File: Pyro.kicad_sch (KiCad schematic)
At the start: 31 parts, among them J12 Conn_01x02_Male, Q1 SSM3K15AMFV,L3F, Q2 BUK9M11-40EX, U6 SiC437BED-T1-GE3, U8 TPS259621DDAT, U9 LTV-247

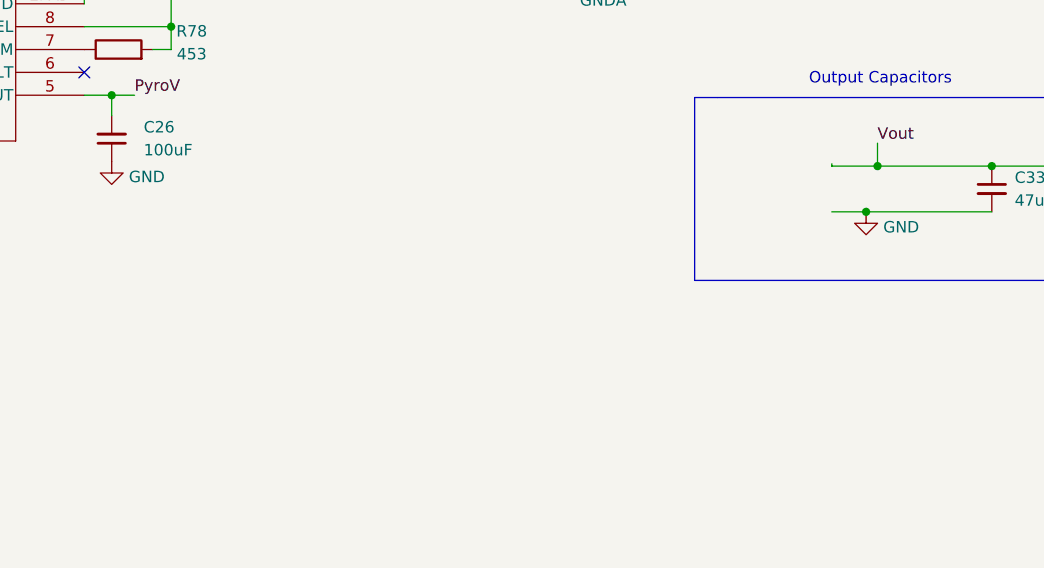
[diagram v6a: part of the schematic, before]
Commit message: added pyro buck caps
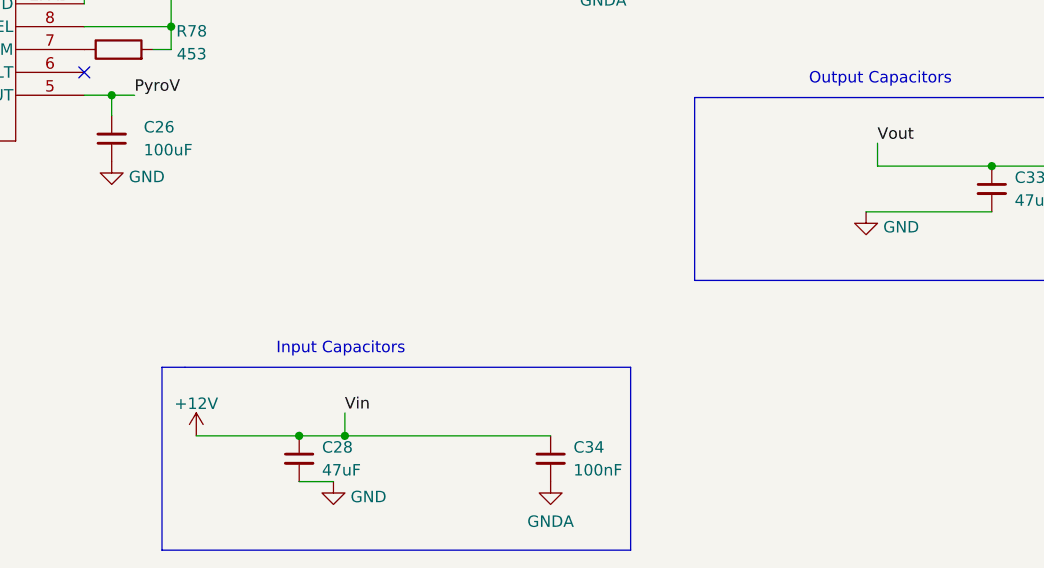
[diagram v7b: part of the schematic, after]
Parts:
- added C28: 47uF, Capacitor_SMD:C_1206_3216Metric, symbol Device:C_Small
- added C34: 100nF, Capacitor_SMD:C_0402_1005Metric, symbol Device:C_Small
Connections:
- net +12V: now also C28.1, C34.1
- net GND: now also C28.2, C34.2
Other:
- note added: "Input Capacitors"
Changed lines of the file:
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@@
   (junction (at 103.378 55.626) (diameter 0) (color 0 0 0 0)
   )
-  (junction (at 186.944 130.302) (diameter 0) (color 0 0 0 0)
-  )
   (junction (at 101.854 122.428) (diameter 0) (color 0 0 0 0)
   )
@@
   (junction (at 157.734 101.092) (diameter 0) (color 0 0 0 0)
   )
+  (junction (at 127.762 160.274) (diameter 0) (color 0 0 0 0)
+  )
   (junction (at 174.244 83.312) (diameter 0) (color 0 0 0 0)
   )
@@
   (junction (at 80.518 32.766) (diameter 0) (color 0 0 0 0)
   )
-  (junction (at 185.674 135.382) (diameter 0) (color 0 0 0 0)
-  )
   (junction (at 28.702 93.218) (diameter 0) (color 0 0 0 0)
   )
@@
   )
   (junction (at 32.004 126.492) (diameter 0) (color 0 0 0 0)
+  )
+  (junction (at 122.682 160.274) (diameter 0) (color 0 0 0 0)
   )
   (junction (at 110.998 73.406) (diameter 0) (color 0 0 0 0)
@@
     (stroke (width 0) (type default))
   )
+  (polyline (pts (xy 159.512 152.654) (xy 159.512 172.974))
+    (stroke (width 0) (type default))
+  )
   (wire (pts (xy 174.244 83.312) (xy 174.244 85.852))
     (stroke (width 0) (type default))
@@
     (stroke (width 0) (type default))
   )
-  (wire (pts (xy 181.864 135.382) (xy 185.674 135.382))
-    (stroke (width 0) (type default))
-  )
   (wire (pts (xy 118.618 72.136) (xy 118.618 73.406))
     (stroke (width 0) (type default))
@@
     (stroke (width 0) (type default))
   )
+  (wire (pts (xy 111.252 160.274) (xy 122.682 160.274))
+    (stroke (width 0) (type default))
+  )
   (wire (pts (xy 245.364 129.032) (xy 245.364 126.492))
     (stroke (width 0) (type default))
@@
     (stroke (width 0) (type default))
   )
-  (wire (pts (xy 181.864 130.048) (xy 181.864 130.302))
-    (stroke (width 0) (type default))
-  )
   (wire (pts (xy 161.544 70.612) (xy 174.244 70.612))
     (stroke (width 0) (type default))
@@
     (stroke (width 0) (type default))
   )
+  (polyline (pts (xy 109.982 152.654) (xy 159.512 152.654))
+    (stroke (width 0) (type default))
+  )
+  (polyline (pts (xy 159.512 172.974) (xy 107.442 172.974))
+    (stroke (width 0) (type default))
+  )
   (wire (pts (xy 231.394 83.312) (xy 230.124 83.312))
     (stroke (width 0) (type default))
   )
+  (wire (pts (xy 127.762 157.734) (xy 127.762 160.274))
+    (stroke (width 0) (type default))
+  )
   (wire (pts (xy 98.806 112.268) (xy 98.806 103.886))
     (stroke (width 0) (type default))
@@
     (stroke (width 0) (type default))
   )
+  (wire (pts (xy 122.682 160.274) (xy 127.762 160.274))
+    (stroke (width 0) (type default))
+  )
   (wire (pts (xy 47.498 63.246) (xy 47.498 64.516))
     (stroke (width 0) (type default))
@@
     (stroke (width 0) (type default))
   )
+  (polyline (pts (xy 107.442 152.654) (xy 109.982 152.654))
+    (stroke (width 0) (type default))
+  )
   (wire (pts (xy 240.284 126.492) (xy 245.364 126.492))
     (stroke (width 0) (type default))
@@
     (stroke (width 0) (type default))
   )
+  (polyline (pts (xy 107.442 172.974) (xy 107.442 152.654))
+    (stroke (width 0) (type default))
+  )
+  (wire (pts (xy 127.762 160.274) (xy 150.622 160.274))
+    (stroke (width 0) (type default))
+  )
   (wire (pts (xy 18.542 93.218) (xy 28.702 93.218))
     (stroke (width 0) (type default))
@@
     (stroke (width 0) (type default))
   )
-  (wire (pts (xy 181.864 130.302) (xy 186.944 130.302))
-    (stroke (width 0) (type default))
-  )
   (wire (pts (xy 23.876 103.886) (xy 23.876 105.41))
     (stroke (width 0) (type default))
@@
   )
   (wire (pts (xy 95.758 55.626) (xy 103.378 55.626))
+    (stroke (width 0) (type default))
+  )
+  (wire (pts (xy 122.682 165.354) (xy 126.492 165.354))
     (stroke (width 0) (type default))
   )
@@
     (effects (font (size 1.27 1.27)) (justify left bottom))
   )
+  (text "Input Capacitors\n" (at 120.142 151.384 0)
+    (effects (font (size 1.27 1.27)) (justify left bottom))
+  )
   (text "Output Capacitors\n" (at 179.324 121.412 0)
     (effects (font (size 1.27 1.27)) (justify left bottom))
@@
   )
   (label "VDD" (at 241.554 75.692 0) (fields_autoplaced)
+    (effects (font (size 1.27 1.27)) (justify left bottom))
+  )
+  (label "Vin" (at 127.762 157.734 0) (fields_autoplaced)
     (effects (font (size 1.27 1.27)) (justify left bottom))
   )
@@
         (path "/7db990e4-92e1-4f99-b4d2-435bbec1ba83/3c6662b6-8783-49dc-b944-3dc2b3e30a07"
           (reference "#PWR0157") (unit 1)
+        )
+      )
+    )
+  )
+  (symbol (lib_id "power:GND") (at 126.492 165.354 0) (unit 1)
+    (in_bom yes) (on_board yes) (dnp no) (fields_autoplaced)
+    (property "Reference" "#PWR064" (at 126.492 171.704 0)
+      (effects (font (size 1.27 1.27)) hide)
+    )
+    (property "Value" "GND" (at 128.397 167.0578 0)
+      (effects (font (size 1.27 1.27)) (justify left))
+    )
+    (property "Footprint" "" (at 126.492 165.354 0)
+      (effects (font (size 1.27 1.27)) hide)
+    )
+    (property "Datasheet" "" (at 126.492 165.354 0)
+      (effects (font (size 1.27 1.27)) hide)
+    )
+    (pin "1")
+    (instances
+      (project "Ricardo-Stark"
+        (path "/7db990e4-92e1-4f99-b4d2-435bbec1ba83/6c17bf58-bab3-4fa6-ad33-cca9e388d73c"
+          (reference "#PWR064") (unit 1)
+        )
+        (path "/7db990e4-92e1-4f99-b4d2-435bbec1ba83/3c6662b6-8783-49dc-b944-3dc2b3e30a07"
+          (reference "#PWR0176") (unit 1)
         )
       )
@@
     )
   )
+  (symbol (lib_id "power:GNDA") (at 150.622 165.354 0) (unit 1)
+    (in_bom yes) (on_board yes) (dnp no) (fields_autoplaced)
+    (property "Reference" "#PWR066" (at 150.622 171.704 0)
+      (effects (font (size 1.27 1.27)) hide)
+    )
+    (property "Value" "GNDA" (at 150.622 169.7974 0)
+      (effects (font (size 1.27 1.27)))
+    )
+    (property "Footprint" "" (at 150.622 165.354 0)
+      (effects (font (size 1.27 1.27)) hide)
+    )
+    (property "Datasheet" "" (at 150.622 165.354 0)
+      (effects (font (size 1.27 1.27)) hide)
+    )
+    (pin "1")
+    (instances
+      (project "Ricardo-Stark"
+        (path "/7db990e4-92e1-4f99-b4d2-435bbec1ba83/6c17bf58-bab3-4fa6-ad33-cca9e388d73c"
+          (reference "#PWR066") (unit 1)
+        )
+        (path "/7db990e4-92e1-4f99-b4d2-435bbec1ba83/3c6662b6-8783-49dc-b944-3dc2b3e30a07"
+          (reference "#PWR0177") (unit 1)
+        )
+      )
+    )
+  )
   (symbol (lib_id "power:GND") (at 221.234 93.472 0) (unit 1)
     (in_bom yes) (on_board yes) (dnp no) (fields_autoplaced)
@@
     )
   )
+  (symbol (lib_id "Device:C_Small") (at 150.622 162.814 0) (unit 1)
+    (in_bom yes) (on_board yes) (dnp no) (fields_autoplaced)
+    (property "Reference" "C34" (at 153.162 161.5503 0)
+      (effects (font (size 1.27 1.27)) (justify left))
+    )
+    (property "Value" "100nF" (at 153.162 164.0903 0)
+      (effects (font (size 1.27 1.27)) (justify left))
+    )
+    (property "Footprint" "Capacitor_SMD:C_0402_1005Metric" (at 150.622 162.814 0)
+      (effects (font (size 1.27 1.27)) hide)
+    )
+    (property "Datasheet" "~" (at 150.622 162.814 0)
+      (effects (font (size 1.27 1.27)) hide)
+    )
+    (pin "1")
+    (pin "2")
+    (instances
+      (project "Ricardo-Stark"
+        (path "/7db990e4-92e1-4f99-b4d2-435bbec1ba83/6c17bf58-bab3-4fa6-ad33-cca9e388d73c"
+          (reference "C34") (unit 1)
+        )
+        (path "/7db990e4-92e1-4f99-b4d2-435bbec1ba83/3c6662b6-8783-49dc-b944-3dc2b3e30a07"
+          (reference "C83") (unit 1)
+        )
+      )
+    )
+  )
   (symbol (lib_id "power:+3V3") (at 98.298 50.546 0) (unit 1)
     (in_bom yes) (on_board yes) (dnp no) (fields_autoplaced)
@@
         )
       )
+    )
+  )
+  (symbol (lib_id "Device:C_Small") (at 122.682 162.814 0) (unit 1)
+    (in_bom yes) (on_board yes) (dnp no) (fields_autoplaced)
+    (property "Reference" "C28" (at 125.222 161.5503 0)
+      (effects (font (size 1.27 1.27)) (justify left))
+    )
+    (property "Value" "47uF" (at 125.222 164.0903 0)
+      (effects (font (size 1.27 1.27)) (justify left))
+    )
+    (property "Footprint" "Capacitor_SMD:C_1206_3216Metric" (at 122.682 162.814 0)
+      (effects (font (size 1.27 1.27)) hide)
+    )
+    (property "Datasheet" "~" (at 122.682 162.814 0)
+      (effects (font (size 1.27 1.27)) hide)
+    )
+    (pin "1")
+    (pin "2")
+    (instances
+      (project "Ricardo-Stark"
+        (path "/7db990e4-92e1-4f99-b4d2-435bbec1ba83/6c17bf58-bab3-4fa6-ad33-cca9e388d73c"
+          (reference "C28") (unit 1)
+        )
+        (path "/7db990e4-92e1-4f99-b4d2-435bbec1ba83/3c6662b6-8783-49dc-b944-3dc2b3e30a07"
+          (reference "C80") (unit 1)
+        )
+      )
+    )
+  )
+  (symbol (lib_id "power:+12V") (at 111.252 160.274 0) (unit 1)
+    (in_bom yes) (on_board yes) (dnp no) (fields_autoplaced)
+    (property "Reference" "#PWR063" (at 111.252 164.084 0)
+      (effects (font (size 1.27 1.27)) hide)
+    )
+    (property "Value" "+12V" (at 111.252 156.6982 0)
+      (effects (font (size 1.27 1.27)))
+    )
+    (property "Footprint" "" (at 111.252 160.274 0)
+      (effects (font (size 1.27 1.27)) hide)
+    )
+    (property "Datasheet" "" (at 111.252 160.274 0)
+      (effects (font (size 1.27 1.27)) hide)
+    )
+    (pin "1")
+    (instances
+      (project "Ricardo-Stark"
+        (path "/7db990e4-92e1-4f99-b4d2-435bbec1ba83/6c17bf58-bab3-4fa6-ad33-cca9e388d73c"
+          (reference "#PWR063") (unit 1)
+        )
+        (path "/7db990e4-92e1-4f99-b4d2-435bbec1ba83/3c6662b6-8783-49dc-b944-3dc2b3e30a07"
+          (reference "#PWR0175") (unit 1)
+        )
+      )

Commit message: Most Review 1 changes made
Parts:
- added C26: 1uF, Capacitor_SMD:C_0402_1005Metric, symbol Device:C_Small
- added R92: 11.52, Resistor_SMD:R_0402_1005Metric, symbol Device:R
- C26: value 100uF -> 1uF; footprint Capacitor_SMD:C_0402_1005Metric -> Capacitor_SMD:C_0603_1608Metric
- U9: value LTV-247 -> 859-LTV-247
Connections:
- net +3V3: now also R92.2
- net EFuse_In: now also C26.1
- net GND: now also R74.1, R75.1, R78.2, C26.2
- net at U8.6 (*FLT): now also R92.1
- net PGOOD: no longer names the net of R19.2, U6.14 (P_GOOD)
- now unconnected: U8.8 (OVLO/OVCSEL)
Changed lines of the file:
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@@
   (junction (at 245.364 126.492) (diameter 0) (color 0 0 0 0)
   )
-  (junction (at 108.458 114.808) (diameter 0) (color 0 0 0 0)
-  )
   (junction (at 157.734 101.092) (diameter 0) (color 0 0 0 0)
   )
@@
   (junction (at 174.244 78.232) (diameter 0) (color 0 0 0 0)
   )
+  (junction (at 37.846 126.492) (diameter 0) (color 0 0 0 0)
+  )
   (junction (at 80.518 32.766) (diameter 0) (color 0 0 0 0)
   )
@@
   )
   (junction (at 110.998 73.406) (diameter 0) (color 0 0 0 0)
+  )
+  (junction (at 108.458 117.348) (diameter 0) (color 0 0 0 0)
   )
   (no_connect (at 174.244 90.932))
   (no_connect (at 174.244 88.392))
-  (no_connect (at 98.806 119.888))
   (no_connect (at 209.804 96.012))
+  (no_connect (at 98.806 114.808))
   (wire (pts (xy 52.578 68.326) (xy 65.278 68.326))
     (stroke (width 0) (type default))
@@
     (stroke (width 0) (type default))
   )
-  (wire (pts (xy 108.458 114.808) (xy 98.806 114.808))
-    (stroke (width 0) (type default))
-  )
   (wire (pts (xy 80.518 32.766) (xy 121.158 32.766))
     (stroke (width 0) (type default))
@@
     (stroke (width 0) (type default))
   )
+  (wire (pts (xy 98.806 119.888) (xy 113.792 119.888))
+    (stroke (width 0) (type default))
+  )
   (wire (pts (xy 209.804 68.072) (xy 219.964 68.072))
     (stroke (width 0) (type default))
@@
     (stroke (width 0) (type default))
   )
-  (wire (pts (xy 108.458 117.348) (xy 108.458 114.808))
-    (stroke (width 0) (type default))
-  )
   (wire (pts (xy 157.734 80.772) (xy 162.814 80.772))
     (stroke (width 0) (type default))
@@
     (stroke (width 0) (type default))
   )
-  (wire (pts (xy 108.458 93.218) (xy 108.458 114.808))
+  (wire (pts (xy 108.458 93.218) (xy 108.458 117.348))
     (stroke (width 0) (type default))
   )
@@
     (effects (font (size 1.27 1.27)) (justify right))
   )
-  (hierarchical_label "PGOOD" (shape output) (at 171.704 98.552 180) (fields_autoplaced)
-    (effects (font (size 1.27 1.27)) (justify right))
-  )
   (hierarchical_label "Nuke 1" (shape input) (at 42.418 63.246 180) (fields_autoplaced)
     (effects (font (size 1.27 1.27)) (justify right))
@@
         (path "/7db990e4-92e1-4f99-b4d2-435bbec1ba83/3c6662b6-8783-49dc-b944-3dc2b3e30a07"
           (reference "R86") (unit 1)
+        )
+      )
+    )
+  )
+  (symbol (lib_id "Device:C_Small") (at 37.846 129.032 0) (unit 1)
+    (in_bom yes) (on_board yes) (dnp no) (fields_autoplaced)
+    (property "Reference" "C26" (at 40.64 127.7683 0)
+      (effects (font (size 1.27 1.27)) (justify left))
+    )
+    (property "Value" "1uF" (at 40.64 130.3083 0)
+      (effects (font (size 1.27 1.27)) (justify left))
+    )
+    (property "Footprint" "Capacitor_SMD:C_0402_1005Metric" (at 37.846 129.032 0)
+      (effects (font (size 1.27 1.27)) hide)
+    )
+    (property "Datasheet" "~" (at 37.846 129.032 0)
+      (effects (font (size 1.27 1.27)) hide)
+    )
+    (pin "1")
+    (pin "2")
+    (instances
+      (project "Ricardo-Stark"
+        (path "/7db990e4-92e1-4f99-b4d2-435bbec1ba83/6c17bf58-bab3-4fa6-ad33-cca9e388d73c"
+          (reference "C26") (unit 1)
+        )
+        (path "/7db990e4-92e1-4f99-b4d2-435bbec1ba83/3c6662b6-8783-49dc-b944-3dc2b3e30a07"
+          (reference "C79") (unit 1)
         )
       )
@@
     )
   )
+  (symbol (lib_id "power:+3.3V") (at 121.412 119.888 0) (unit 1)
+    (in_bom yes) (on_board yes) (dnp no)
+    (property "Reference" "#PWR09" (at 121.412 123.698 0)
+      (effects (font (size 1.27 1.27)) hide)
+    )
+    (property "Value" "+3.3V" (at 121.793 115.4938 0)
+      (effects (font (size 1.27 1.27)))
+    )
+    (property "Footprint" "" (at 121.412 119.888 0)
+      (effects (font (size 1.27 1.27)) hide)
+    )
+    (property "Datasheet" "" (at 121.412 119.888 0)
+      (effects (font (size 1.27 1.27)) hide)
+    )
+    (pin "1")
+    (instances
+      (project "Ricardo-Stark"
+        (path "/7db990e4-92e1-4f99-b4d2-435bbec1ba83"
+          (reference "#PWR09") (unit 1)
+        )
+        (path "/7db990e4-92e1-4f99-b4d2-435bbec1ba83/3c6662b6-8783-49dc-b944-3dc2b3e30a07"
+          (reference "#PWR0178") (unit 1)
+        )
+      )
+    )
+  )
   (symbol (lib_id "power:GNDA") (at 209.804 65.532 90) (unit 1)
     (in_bom yes) (on_board yes) (dnp no) (fields_autoplaced)
@@
     )
   )
+  (symbol (lib_id "power:GND") (at 108.458 117.348 0) (unit 1)
+    (in_bom yes) (on_board yes) (dnp no) (fields_autoplaced)
+    (property "Reference" "#PWR048" (at 108.458 123.698 0)
+      (effects (font (size 1.27 1.27)) hide)
+    )
+    (property "Value" "GND" (at 110.363 119.0518 0)
+      (effects (font (size 1.27 1.27)) (justify left))
+    )
+    (property "Footprint" "" (at 108.458 117.348 0)
+      (effects (font (size 1.27 1.27)) hide)
+    )
+    (property "Datasheet" "" (at 108.458 117.348 0)
+      (effects (font (size 1.27 1.27)) hide)
+    )
+    (pin "1")
+    (instances
+      (project "Ricardo-Stark"
+        (path "/7db990e4-92e1-4f99-b4d2-435bbec1ba83/6c17bf58-bab3-4fa6-ad33-cca9e388d73c"
+          (reference "#PWR048") (unit 1)
+        )
+        (path "/7db990e4-92e1-4f99-b4d2-435bbec1ba83/3c6662b6-8783-49dc-b944-3dc2b3e30a07"
+          (reference "#PWR0180") (unit 1)
+        )
+      )
+    )
+  )
   (symbol (lib_id "Device:R_Small") (at 223.774 61.722 180) (unit 1)
     (in_bom yes) (on_board yes) (dnp no)
@@
     )
   )
+  (symbol (lib_id "Device:R") (at 117.602 119.888 90) (unit 1)
+    (in_bom yes) (on_board yes) (dnp no)
+    (property "Reference" "R92" (at 125.73 117.856 90)
+      (effects (font (size 1.27 1.27)))
+    )
+    (property "Value" "11.52" (at 125.73 120.396 90)
+      (effects (font (size 1.27 1.27)))
+    )
+    (property "Footprint" "Resistor_SMD:R_0402_1005Metric" (at 117.602 121.666 90)
+      (effects (font (size 1.27 1.27)) hide)
+    )
+    (property "Datasheet" "~" (at 117.602 119.888 0)
+      (effects (font (size 1.27 1.27)) hide)
+    )
+    (pin "1")
+    (pin "2")
+    (instances
+      (project "Ricardo-Stark"
+        (path "/7db990e4-92e1-4f99-b4d2-435bbec1ba83/3c6662b6-8783-49dc-b944-3dc2b3e30a07"
+          (reference "R92") (unit 1)
+        )
+      )
+    )
+  )
   (symbol (lib_id "power:GND") (at 162.814 93.472 0) (unit 1)
     (in_bom yes) (on_board yes) (dnp no)
@@
       (effects (font (size 1.27 1.27)))
     )
-    (property "Value" "LTV-247" (at 110.998 46.99 0)
+    (property "Value" "859-LTV-247" (at 110.998 46.99 0)
       (effects (font (size 1.27 1.27)))
     )
@@
   (symbol (lib_id "Device:R") (at 102.616 117.348 90) (unit 1)
     (in_bom yes) (on_board yes) (dnp no)
-    (property "Reference" "R78" (at 110.744 115.316 90)
-      (effects (font (size 1.27 1.27)))
-    )
-    (property "Value" "453" (at 110.744 117.856 90)
+    (property "Reference" "R78" (at 103.124 113.03 90)
+      (effects (font (size 1.27 1.27)))
+    )
+    (property "Value" "453" (at 102.87 114.808 90)
       (effects (font (size 1.27 1.27)))
     )
@@
       (effects (font (size 1.27 1.27)) (justify right))
     )
-    (property "Value" "100uF" (at 105.41 128.5176 0)
+    (property "Value" "1uF" (at 105.41 128.5176 0)
       (effects (font (size 1.27 1.27)) (justify right))
     )
-    (property "Footprint" "Capacitor_SMD:C_0402_1005Metric" (at 101.854 127.254 0)
+    (property "Footprint" "Capacitor_SMD:C_0603_1608Metric" (at 101.854 127.254 0)
       (effects (font (size 1.27 1.27)) hide)
     )
@@
         )
       )
+    )
+  )
+  (symbol (lib_id "power:GND") (at 37.846 131.572 0) (unit 1)
+    (in_bom yes) (on_board yes) (dnp no)
+    (property "Reference" "#PWR0179" (at 37.846 137.922 0)
+      (effects (font (size 1.27 1.27)) hide)
+    )
+    (property "Value" "GND" (at 37.846 136.652 0)
+      (effects (font (size 1.27 1.27)))
+    )
+    (property "Footprint" "" (at 37.846 131.572 0)
+      (effects (font (size 1.27 1.27)) hide)
+    )
+    (property "Datasheet" "" (at 37.846 131.572 0)
+      (effects (font (size 1.27 1.27)) hide)
+    )
+    (pin "1")
+    (instances
+      (project "Ricardo-Stark"
+        (path "/7db990e4-92e1-4f99-b4d2-435bbec1ba83/3c6662b6-8783-49dc-b944-3dc2b3e30a07"
+          (reference "#PWR0179") (unit 1)
+        )
+      )
